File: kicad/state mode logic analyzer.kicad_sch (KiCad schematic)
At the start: 139 parts, among them J1 USB_B_Micro, J10 5V USB1, J2 USB_B_Micro, J3 CLK 0-7, J4 8-15, J5 16-23, J6 24-31, J7 SWD0, J8 SWD1, J9 5V USB0, SW1 Reset 0, SW2 Boot 0, SW3 Reset 1, SW4 Boot 1, U1 RP2040, U2 RP2040, U3 74HC4520D, U4 LTC6994xS6-1, U5 MCP4725, U6 AD5241-1M, U7 IS25LP128F-JBLE, U8 IS25LP128F-JBLE, U9 MCP1826S, Y1 ECS-120-18-33-JEM-TR, Y2 ECS-120-18-33-JEM-TR

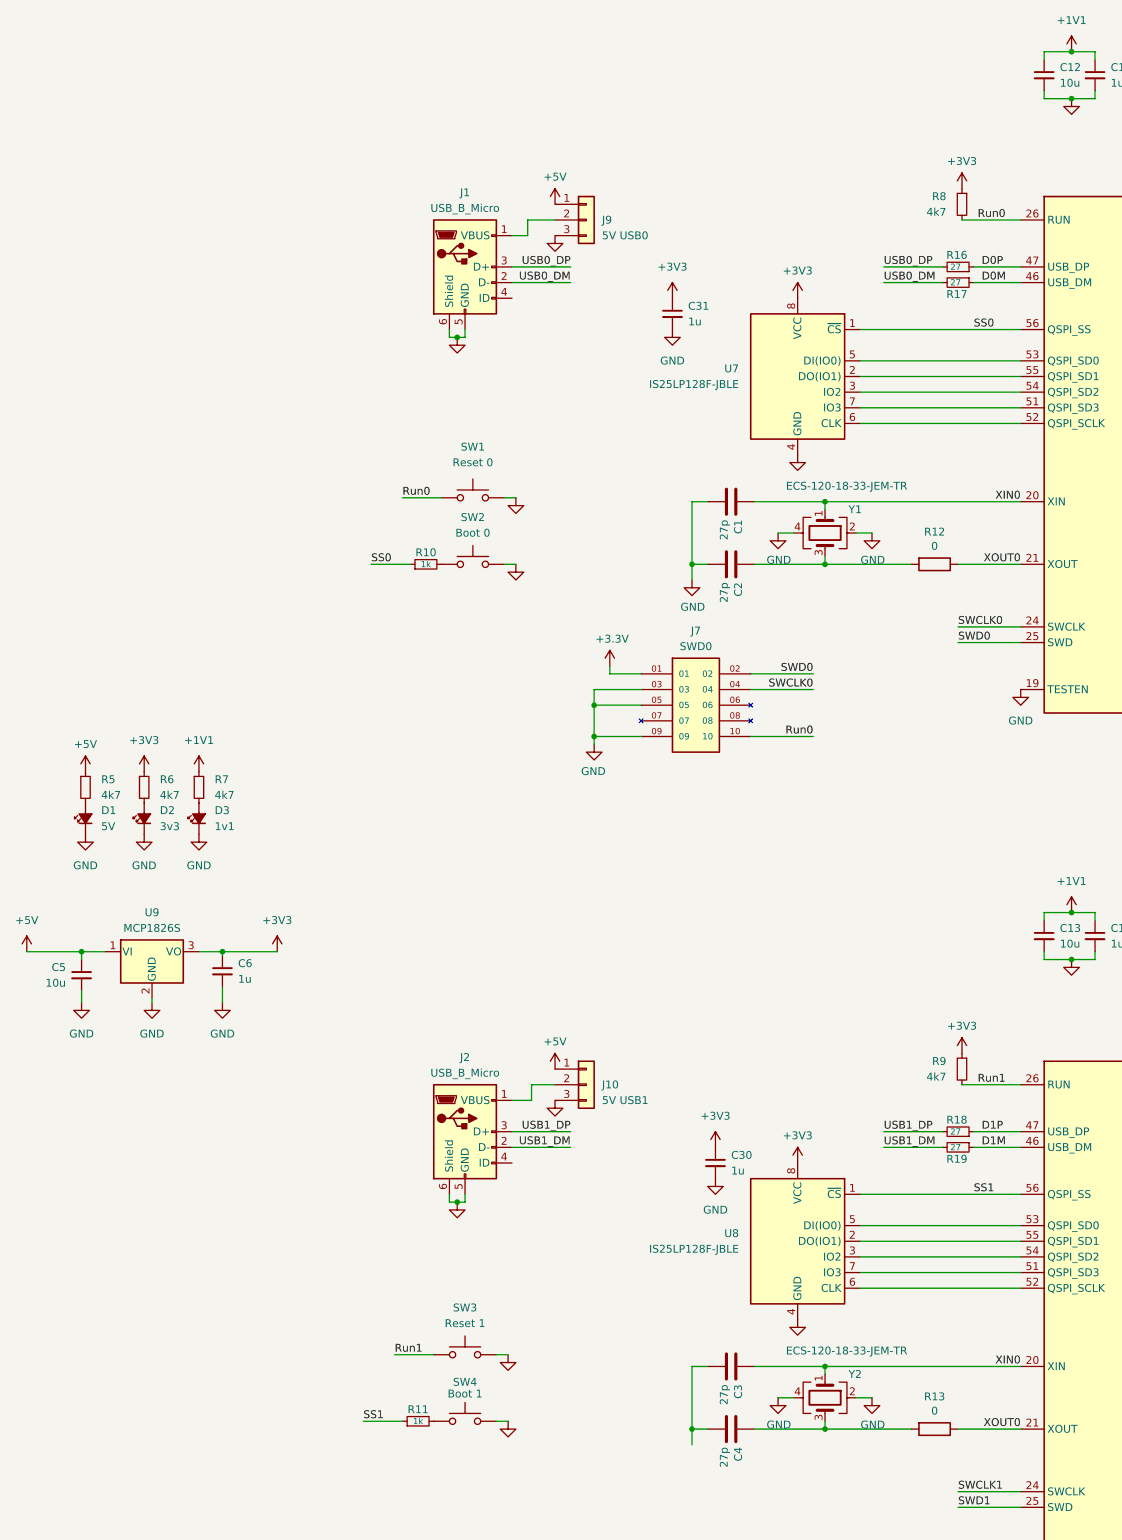
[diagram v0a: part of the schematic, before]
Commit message: switched to usb-c
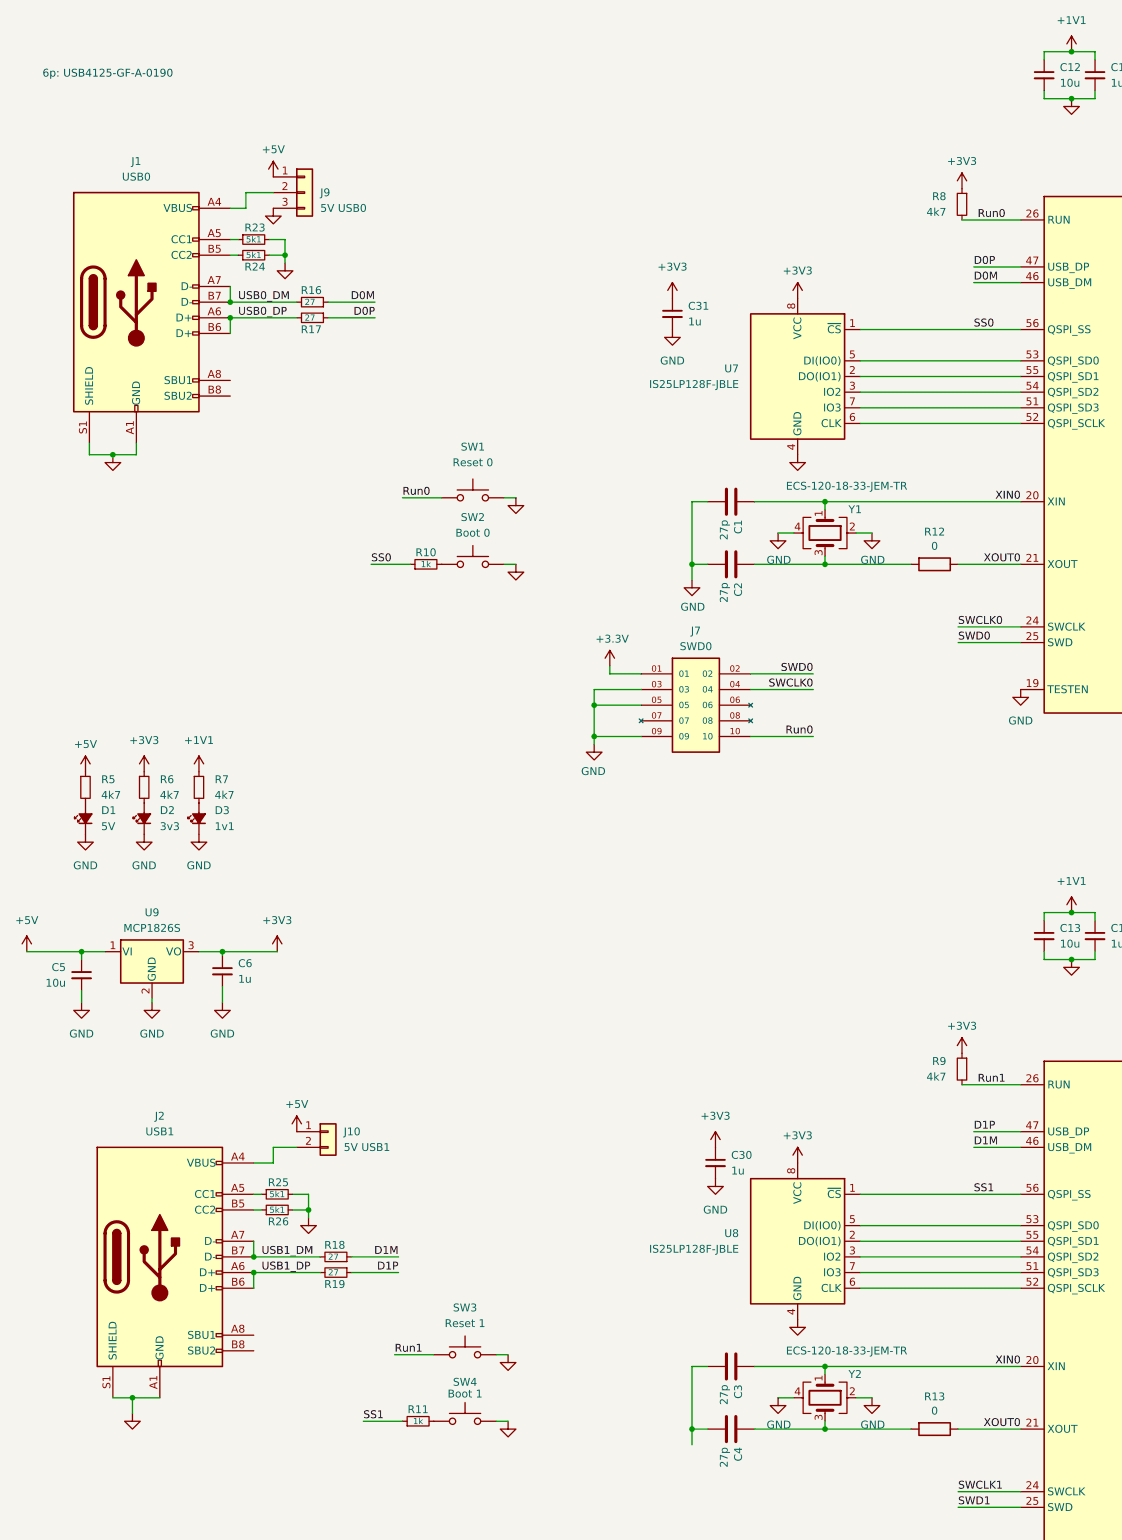
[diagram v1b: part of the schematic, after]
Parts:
- removed J1, J2: USB_B_Micro, Connector_USB:USB_Micro-B_GCT_USB3076-30-A, symbol Connector:USB_B_Micro
- added J1: USB0, Connector_USB:USB_C_Receptacle_GCT_USB4105-xx-A_16P_TopMnt_Horizontal, symbol Connector:USB_C_Receptacle_USB2.0
- added J2: USB1, Connector_USB:USB_C_Receptacle_GCT_USB4105-xx-A_16P_TopMnt_Horizontal, symbol Connector:USB_C_Receptacle_USB2.0
- added R23, R24, R25, R26: 5k1, Resistor_SMD:R_0603_1608Metric_Pad0.98x0.95mm_HandSolder, symbol Device:R_Small
- J10: footprint Connector_PinHeader_2.54mm:PinHeader_1x03_P2.54mm_Vertical -> Connector_PinHeader_2.54mm:PinHeader_1x02_P2.54mm_Vertical; symbol Connector_Generic:Conn_01x03 -> Connector_Generic:Conn_01x02
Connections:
- net D0M: now also R16.1; no longer R17.1
- net D0P: now also R17.1; no longer R16.1
- net D1M: now also R18.1; no longer R19.1
- net D1P: now also R19.1; no longer R18.1
- net GND: now also J1.A1 (GND), J1.A12 (GND), J1.B1 (GND), J1.B12 (GND), J1.S1 (SHIELD), J2.A1 (GND), J2.A12 (GND), J2.B1 (GND), J2.B12 (GND), J2.S1 (SHIELD), R23.2, R24.2, R25.2, R26.2; no longer J10.3 (Pin_3)
- net USB0_DM: now also R16.2, J1.A7 (D-), J1.B7 (D-); no longer R17.2
- net USB0_DP: now also R17.2, J1.A6 (D+), J1.B6 (D+); no longer R16.2
- net USB1_DM: now also R18.2, J2.A7 (D-), J2.B7 (D-); no longer R19.2
- net USB1_DP: now also R19.2, J2.A6 (D+), J2.B6 (D+); no longer R18.2
- net at J10.2 (Pin_2): now also J2.A4 (VBUS), J2.A9 (VBUS), J2.B4 (VBUS), J2.B9 (VBUS)
- net at J9.2 (Pin_2): now also J1.A4 (VBUS), J1.A9 (VBUS), J1.B4 (VBUS), J1.B9 (VBUS)
- new net: J1.A5 (CC1), R23.1
- new net: J2.A5 (CC1), R25.1
- new net: J2.B5 (CC2), R26.1
- new net: J1.B5 (CC2), R24.1
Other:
- note added: "6p: USB4125-GF-A-0190"
- moved on the sheet: J9, R18, R19

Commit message: passed erc for first schem ver
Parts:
- added TP15: TestPoint_Harwin, My Libraries:Harwin-S1751-46-Test-Point, symbol My Library:TestPoint_Harwin
- J7, J8: symbol FTSH-105-XX-X-DV:FTSH-105-XX-X-DV -> My Library:SWD_with_FTSH-105-XX-X-DV
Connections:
- net +1V1: no longer C13.1, C14.1, U2.23 (DVDD), U2.45 (VREG_VOUT), U2.50 (DVDD)
- net CNT_CLK: now also U3.1 (CK)
- net CNT_RESET: now also U3.15 (Reset), U3.7 (Reset)
- net at U1.39 (GPIO27_ADC1): now also TP15.1
- new net +1V1-other: C13.1, C14.1, U2.23 (DVDD), U2.45 (VREG_VOUT), U2.50 (DVDD)
- no-connect marks 0 -> 4

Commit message: floor planning ongoing
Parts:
- removed C13, C18: 10u, Capacitor_SMD:C_0805_2012Metric, symbol My Library:C_0805
- removed C14, C15, C16, C17, C26, C27, C28, C29, C30: 1u, Capacitor_SMD:C_0603_1608Metric_Pad1.08x0.95mm_HandSolder, symbol Device:C_Small
- removed C3, C4: 27p, Capacitor_SMD:C_0603_1608Metric, symbol Device:C
- removed D7: 2040_L1, LED_SMD:LED_1206_3216Metric_Pad1.42x1.75mm_HandSolder, symbol Device:LED_Small_Filled
- removed J10: 5V USB1, Connector_PinHeader_2.54mm:PinHeader_1x02_P2.54mm_Vertical, symbol Connector_Generic:Conn_01x02
- removed J2: USB1, Connector_USB:USB_C_Receptacle_GCT_USB4105-xx-A_16P_TopMnt_Horizontal, symbol Connector:USB_C_Receptacle_USB2.0
- removed J6: 24-31, Connector_PinHeader_2.54mm:PinHeader_2x10_P2.54mm_Vertical, symbol Connector_Generic:Conn_02x10_Odd_Even
- removed J8: SWD1, FTSH-105-01-L-DV-K:SAMTEC_FTSH-105-XX-X-DV, symbol My Library:SWD_with_FTSH-105-XX-X-DV
- removed R11, R15: 1k, Resistor_SMD:R_0603_1608Metric_Pad0.98x0.95mm_HandSolder, symbol Device:R_Small
- removed R18, R19: 27, Resistor_SMD:R_0603_1608Metric_Pad0.98x0.95mm_HandSolder, symbol Device:R_Small
- removed R9: 4k7, Resistor_SMD:R_0603_1608Metric_Pad0.98x0.95mm_HandSolder, symbol Device:R_Small
- removed SW3: Reset 1, Button_Switch_SMD:SW_SPST_PTS810, symbol Switch:SW_Push
- removed SW4: Boot 1, Button_Switch_SMD:SW_SPST_PTS810, symbol Switch:SW_Push
- removed TP116, TP117, TP118, TP119, TP120, TP121, TP122, TP123, TP124, TP125, TP126, TP127, TP128, TP129, TP130, TP131, TP132: TestPoint_Harwin, My Libraries:Harwin-S1751-46-Test-Point, symbol My Library:TestPoint_Harwin
- removed U2: RP2040, Package_DFN_QFN:QFN-56-1EP_7x7mm_P0.4mm_EP3.2x3.2mm, symbol MCU_RaspberryPi:RP2040
- removed U8: IS25LP128F-JBLE, Package_SO:SOIC-8_5.23x5.23mm_P1.27mm, symbol Memory_Flash:W25Q128JVS
- removed Y2: ECS-120-18-33-JEM-TR, Crystal:Crystal_SMD_3225-4Pin_3.2x2.5mm, symbol Device:Crystal_GND24
- added C3, C4: 1u, Capacitor_SMD:C_0603_1608Metric_Pad1.08x0.95mm_HandSolder, symbol Device:C_Small
- added D7: BZA856AVL, Package_TO_SOT_SMD:SOT-353_SC-70-5, symbol Power_Protection:SP0504BAJT
- added J2: Exp Out, Connector_PinHeader_2.54mm:PinHeader_2x10_P2.54mm_Horizontal, symbol Connector_Generic:Conn_02x10_Odd_Even
- added JP6: CLK Bypass, Jumper:SolderJumper-2_P1.3mm_Bridged2Bar_Pad1.0x1.5mm, symbol Jumper:Jumper_2_Bridged
- added R11, R15, R18, R19, R9: 0, Resistor_SMD:R_0603_1608Metric_Pad0.98x0.95mm_HandSolder, symbol Device:R
- added R27, R28, R29, R30, R31, R32, R33, R34, R35, R36, R37, R38, R39, R40: 220, Resistor_SMD:R_0603_1608Metric, symbol Device:R_Small
- added TP16, TP17, TP18, TP19: TestPoint_Harwin, My Libraries:Harwin-S1751-46-Test-Point, symbol My Library:TestPoint_Harwin
- added U2, U8: 74LVC244, Package_SO:TSSOP-20_4.4x6.5mm_P0.65mm, symbol 74xx:74HC244
- J5: value 16-23 -> Exp In; footprint Connector_PinHeader_2.54mm:PinHeader_2x10_P2.54mm_Vertical -> Connector_PinSocket_2.54mm:PinSocket_2x10_P2.54mm_Horizontal
- R25, R26: value 5k1 -> 220; footprint Resistor_SMD:R_0603_1608Metric_Pad0.98x0.95mm_HandSolder -> Resistor_SMD:R_0603_1608Metric
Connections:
- net IN16 is gone; now on net TS1: J5.3 (Pin_3)
- net IN17 is gone; now on net TS2: J5.5 (Pin_5)
- net IN18 is gone; now on net TS3: J5.7 (Pin_7)
- net IN19 is gone; now on net TS4: J5.9 (Pin_9)
- net IN20 is gone; now on net TS5: J5.11 (Pin_11)
- net IN21 is gone; now on net TS6: J5.13 (Pin_13)
- net IN22 is gone; now on net TS7: J5.15 (Pin_15)
- net IN23 is gone; now on net SDA: J5.17 (Pin_17)
- net +3V3: now also C3.1, C4.1, U2.20 (VCC), U8.20 (VCC); no longer J5.19 (Pin_19)
- net +5V: no longer J5.1 (Pin_1)
- net CLK: now also J5.2 (Pin_2), J2.2 (Pin_2), JP6.1 (A)
- net CNT_CLK: now also TP15.1, U1.39 (GPIO27_ADC1), R9.2; no longer TP10.1, U3.1 (CK)
- net CNT_RESET: now also R14.1, U1.40 (GPIO28_ADC2), R11.2; no longer TP11.1, U3.15 (Reset), U3.7 (Reset)
- net GND: now also C3.2, C4.2, D7.2 (A), TP16.1, TP17.1, TP18.1, TP19.1, U2.1 (1OE), U2.10 (GND), U2.19 (2OE), U8.1 (1OE), U8.10 (GND), U8.19 (2OE); no longer J5.10 (Pin_10), J5.12 (Pin_12), J5.14 (Pin_14), J5.16 (Pin_16), J5.18 (Pin_18), J5.2 (Pin_2), J5.20 (Pin_20), J5.4 (Pin_4), J5.6 (Pin_6), J5.8 (Pin_8), R25.2, R26.2
- net IN00: now also R25.1; no longer TP100.1, U1.5 (GPIO3)
- net IN01: now also R26.1; no longer TP101.1, U1.6 (GPIO4)
- net IN02: now also R27.1; no longer TP102.1, U1.7 (GPIO5)
- net IN03: now also R28.1; no longer TP103.1, U1.8 (GPIO6)
- net IN04: now also R29.1; no longer TP104.1, U1.9 (GPIO7)
- net IN05: now also R30.1; no longer TP105.1, U1.11 (GPIO8)
- net IN06: now also R31.1; no longer TP106.1, U1.12 (GPIO9)
- net IN07: now also R32.1; no longer TP107.1, U1.13 (GPIO10)
- net IN08: now also R33.1; no longer TP108.1, U1.14 (GPIO11)
- net IN09: now also R34.1; no longer TP109.1, U1.15 (GPIO12)
- net IN10: now also R35.1; no longer TP110.1, U1.16 (GPIO13)
- net IN11: now also R36.1; no longer TP111.1, U1.17 (GPIO14)
- net IN12: now also R37.1; no longer TP112.1, U1.18 (GPIO15)
- net IN13: now also R38.1; no longer TP113.1, U1.27 (GPIO16)
- net IN14: now also R39.1; no longer TP114.1, U1.28 (GPIO17)
- net IN15: now also R40.1; no longer TP115.1, U1.29 (GPIO18)
- net IN_CLK: now also JP6.2 (B)
- net LA_Enable: now also J5.4 (Pin_4), J2.4 (Pin_4)
- net SCL: now also J5.19 (Pin_19), R13.2, J2.19 (Pin_19), R18.2; no longer U5.5 (SCL), U6.6 (SCL)
- net SDA: now also J2.17 (Pin_17), R15.2, R19.2; no longer U5.4 (SDA), U6.7 (SDA)
- net TS0: now also J5.1 (Pin_1), J2.1 (Pin_1)
- net TS1: now also J2.3 (Pin_3)
- net TS2: now also J2.5 (Pin_5)
- net TS3: now also J2.7 (Pin_7)
- net TS4: now also J2.9 (Pin_9)
- net TS5: now also J2.11 (Pin_11)
- net TS6: now also J2.13 (Pin_13)
- net TS7: now also J2.15 (Pin_15)
- net USB0_DM: now also D7.5 (K)
- net USB0_DP: now also D7.4 (K)
- net XOUT0: no longer R13.1
- net VBUS: now reaches J1.A4 (VBUS), J1.A9 (VBUS), J1.B4 (VBUS), J1.B9 (VBUS), J9.2 (Pin_2)
- net VBUS: now also D7.3 (K)
- new net: R33.2, U2.2 (1A0)
- new net: R18.1, U5.5 (SCL)
- new net: R28.2, U8.8 (1A3)
- new net: R32.2, U8.11 (2A3)
- new net: R27.2, U8.6 (1A2)
- new net: R34.2, U2.4 (1A1)
- new net: R13.1, U6.6 (SCL)
- new net: R31.2, U8.13 (2A2)
- new net: R30.2, U8.15 (2A1)
- new net: R29.2, U8.17 (2A0)
- new net: R25.2, U8.2 (1A0)
- new net: R26.2, U8.4 (1A1)
- new net: R9.1, TP10.1, U3.1 (CK)
- new net: R11.1, TP11.1, U3.15 (Reset), U3.7 (Reset)
- new net: R19.1, U5.4 (SDA)
- new net: R39.2, U2.13 (2A2)
- new net: R36.2, U2.8 (1A3)
- new net: R35.2, U2.6 (1A2)
- new net: R37.2, U2.17 (2A0)
- new net: R15.1, U6.7 (SDA)
- new net: R40.2, U2.11 (2A3)
- new net: R38.2, U2.15 (2A1)
- new net BUF00: TP100.1, U1.5 (GPIO3), U8.18 (1Y0)
- new net BUF01: TP101.1, U1.6 (GPIO4), U8.16 (1Y1)
- new net BUF02: TP102.1, U1.7 (GPIO5), U8.14 (1Y2)
- new net BUF03: TP103.1, U1.8 (GPIO6), U8.12 (1Y3)
- new net BUF04: TP104.1, U1.9 (GPIO7), U8.3 (2Y0)
- new net BUF05: TP105.1, U1.11 (GPIO8), U8.5 (2Y1)
- new net BUF06: TP106.1, U1.12 (GPIO9), U8.7 (2Y2)
- new net BUF07: TP107.1, U1.13 (GPIO10), U8.9 (2Y3)
- new net BUF08: TP108.1, U1.14 (GPIO11), U2.18 (1Y0)
- new net BUF09: TP109.1, U1.15 (GPIO12), U2.16 (1Y1)
- new net BUF10: TP110.1, U1.16 (GPIO13), U2.14 (1Y2)
- new net BUF11: TP111.1, U1.17 (GPIO14), U2.12 (1Y3)
- new net BUF12: TP112.1, U1.18 (GPIO15), U2.3 (2Y0)
- new net BUF13: TP113.1, U1.27 (GPIO16), U2.5 (2Y1)
- new net BUF14: TP114.1, U1.28 (GPIO17), U2.7 (2Y2)
- new net BUF15: TP115.1, U1.29 (GPIO18), U2.9 (2Y3)
- no-connect marks 4 -> 19
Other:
- note added: "BZA856AVL"
- note removed: "6p: USB4125-GF-A-0190"
- note removed: "Newark has TSSOP only"
- moved on the sheet: C1, C10, C11, C12, C19, C2, C20, C21, C22, C23, C24, C25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

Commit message: going to re-order all the IOs
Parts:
- removed TP15: TestPoint_Harwin, My Libraries:Harwin-S1751-46-Test-Point, symbol My Library:TestPoint_Harwin
- removed U2, U8: 74LVC244, Package_SO:TSSOP-20_4.4x6.5mm_P0.65mm, symbol 74xx:74HC244
- added C13: 1u, Capacitor_SMD:C_0603_1608Metric_Pad1.08x0.95mm_HandSolder, symbol Device:C_Small
- added U10, U11: 74LVC245APW, Package_SO:TSSOP-20_4.4x6.5mm_P0.65mm, symbol 74xx:74HC245
- JP6: footprint Jumper:SolderJumper-2_P1.3mm_Bridged2Bar_Pad1.0x1.5mm -> Jumper:SolderJumper-2_P1.3mm_Open_Pad1.0x1.5mm; symbol Jumper:Jumper_2_Bridged -> Jumper:Jumper_2_Open
- U6: value AD5241-1M -> AD5241BRZ1M; footprint Package_SO:SOIC-16_3.9x9.9mm_P1.27mm -> Package_SO:SOIC-14_3.9x8.7mm_P1.27mm; SPN (none) -> 49AK9193
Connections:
- net +3V3: now also C13.1, U10.1 (A->B), U10.20 (VCC), U11.1 (A->B), U11.20 (VCC)
- net BUF00: now also U1.29 (GPIO18), U10.11 (B7); no longer U1.5 (GPIO3)
- net BUF01: now also U1.28 (GPIO17), U10.12 (B6); no longer U1.6 (GPIO4)
- net BUF02: now also U1.27 (GPIO16), U10.13 (B5); no longer U1.7 (GPIO5)
- net BUF03: now also U1.18 (GPIO15), U10.14 (B4); no longer U1.8 (GPIO6)
- net BUF04: now also U1.17 (GPIO14), U10.15 (B3); no longer U1.9 (GPIO7)
- net BUF05: now also U1.16 (GPIO13), U10.16 (B2); no longer U1.11 (GPIO8)
- net BUF06: now also U1.15 (GPIO12), U10.17 (B1); no longer U1.12 (GPIO9)
- net BUF07: now also U1.14 (GPIO11), U10.18 (B0); no longer U1.13 (GPIO10)
- net BUF08: now also U1.13 (GPIO10), U11.11 (B7); no longer U1.14 (GPIO11)
- net BUF09: now also U1.12 (GPIO9), U11.12 (B6); no longer U1.15 (GPIO12)
- net BUF10: now also U1.11 (GPIO8), U11.13 (B5); no longer U1.16 (GPIO13)
- net BUF11: now also U1.9 (GPIO7), U11.14 (B4); no longer U1.17 (GPIO14)
- net BUF12: now also U1.8 (GPIO6), U11.15 (B3); no longer U1.18 (GPIO15)
- net BUF13: now also U1.7 (GPIO5), U11.16 (B2); no longer U1.27 (GPIO16)
- net BUF14: now also U1.6 (GPIO4), U11.17 (B1); no longer U1.28 (GPIO17)
- net BUF15: now also U1.5 (GPIO3), U11.18 (B0); no longer U1.29 (GPIO18)
- net CLK: now also J2.1 (Pin_1), J5.1 (Pin_1); no longer J2.2 (Pin_2), J5.2 (Pin_2)
- net GND: now also J2.10 (Pin_10), J2.12 (Pin_12), J2.14 (Pin_14), J2.16 (Pin_16), J2.18 (Pin_18), J2.2 (Pin_2), J2.6 (Pin_6), J2.8 (Pin_8), J5.10 (Pin_10), J5.12 (Pin_12), J5.14 (Pin_14), J5.16 (Pin_16), J5.18 (Pin_18), J5.2 (Pin_2), J5.6 (Pin_6), J5.8 (Pin_8), U9.4 (GND), C13.2, U10.10 (GND), U10.19 (CE), U11.10 (GND), U11.19 (CE)
- net SDA: now also J2.20 (Pin_20), J5.20 (Pin_20); no longer J2.17 (Pin_17), J5.17 (Pin_17)
- net TS0: now also J2.3 (Pin_3), J5.3 (Pin_3); no longer J2.1 (Pin_1), J5.1 (Pin_1)
- net TS1: now also J2.5 (Pin_5), J5.5 (Pin_5); no longer J2.3 (Pin_3), J5.3 (Pin_3)
- net TS2: now also J2.7 (Pin_7), J5.7 (Pin_7); no longer J2.5 (Pin_5), J5.5 (Pin_5)
- net TS3: now also J2.9 (Pin_9), J5.9 (Pin_9); no longer J2.7 (Pin_7), J5.7 (Pin_7)
- net TS4: now also J2.11 (Pin_11), J5.11 (Pin_11); no longer J2.9 (Pin_9), J5.9 (Pin_9)
- net TS5: now also J2.13 (Pin_13), J5.13 (Pin_13); no longer J2.11 (Pin_11), J5.11 (Pin_11)
- net TS6: now also J2.15 (Pin_15), J5.15 (Pin_15); no longer J2.13 (Pin_13), J5.13 (Pin_13)
- net TS7: now also J2.17 (Pin_17), J5.17 (Pin_17); no longer J2.15 (Pin_15), J5.15 (Pin_15)
- net A8: now reaches R33.2
- net A8: now also U11.9 (A7)
- net A3: now reaches R28.2
- net A3: now also U10.6 (A4)
- net A7: now reaches R32.2
- net A7: now also U10.2 (A0)
- net A2: now reaches R27.2
- net A2: now also U10.7 (A5)
- net W: now reaches JP5.1 (A), TP14.1, U6.2 (W)
- net A9: now reaches R34.2
- net A9: now also U11.8 (A6)
- net A6: now reaches R31.2
- net A6: now also U10.3 (A1)
- net A5: now reaches R30.2
- net A5: now also U10.4 (A2)
- net A4: now reaches R29.2
- net A4: now also U10.5 (A3)
- net A0: now reaches R25.2
- net A0: now also U10.9 (A7)
- net A1: now reaches R26.2
- net A1: now also U10.8 (A6)
- net A14: now reaches R39.2
- net A14: now also U11.3 (A1)
- net A11: now reaches R36.2
- net A11: now also U11.6 (A4)
- net A10: now reaches R35.2
- net A10: now also U11.7 (A5)
- net A12: now reaches R37.2
- net A12: now also U11.5 (A3)
- net A15: now reaches R40.2
- net A15: now also U11.2 (A0)
- net A13: now reaches R38.2
- net A13: now also U11.4 (A2)
- net D0M renamed DN
- net D0P renamed DP
- net Run0 renamed Run
- net SS0 renamed ~{CS}
- net SWCLK0 renamed SWCLK
- net SWD0 renamed SWD
- net USB0_DM renamed USB_DN
- net USB0_DP renamed USB_DP
- net XIN0 renamed XIN
- net XOUT0 renamed XOUT
- no-connect marks 19 -> 3
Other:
- note added: "Added hidden Pin 4 to MCP1826S Symbol"
- note removed: "BZA856AVL"
- moved on the sheet: C3, C4, TP100, TP101, TP102, TP103, TP104, TP105, TP106, TP107, TP108, TP109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
